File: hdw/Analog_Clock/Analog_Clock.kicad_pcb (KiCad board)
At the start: 2 copper layers, 427 parts, among them J1301 USB_B_Mini, J201 +12V IN, J2401 I2C, J2402 USB UART, J2403 DAC SPI, J801 PICKIT4, Q1601 BSS214NW, Q2401 BSS214NW, Q401 BSS214NW, Q402 ZXMS6004FFTA, Q601 FDC5612, Q801 BSS214NW, SW2201 Cap_Touch, SW2202 Cap_Touch, SW801 MRST, U1001 PIC32MZ0512EFE064T-I_PT, U1201 DS3231MZ, U1301 TLV6700, U1302 FT234XD, U1303 74LVC1G17, U1304 TXB0102DCU, U1305 TPD3S014DBVR, U1401 INA219BxDCN, U1402 MCP9804, U1501 DS1683, U1601 74LVC1G06, U1602 74LVC1G06, U1603 LP2985-3.3, U1604 74LVC1G06, U1605 74LVC1G07, U1606 74LVC1G06, U1701 74LVC1G06, U1702 74LVC1G06, U1703 74LVC1G06, U1704 74LVC1G06, U1801 74LVC1G07, U1802 LT1790-2.048, U1803 DAC8551, U1804 OPA2197xDGK, U1901 74LVC1G07, U1902 LT1790-2.048, U1903 DAC8551, U1904 OPA2197xDGK, U2001 74LVC1G07, U2002 LT1790-2.048, U2003 DAC8551, U2004 OPA2197xDGK, U201 TPS26600RHFT, U2101 LP5009, U2201 AT42QT1010-TSHR, U2202 AT42QT1010-TSHR, U2203 74LVC1G17, U2204 74LVC1G17, U2301 74LVC1G06, U2302 74LVC1G06, U2303 74LVC1G06, U2304 74LVC1G06, U2401 LTC6900, U2402 74LVC1G08, U2403 MCP9804, U301 INA219BxDCN, U302 MCP9804, U401 TPS62150, U501 INA219BxDCN, U502 MCP9804, U601 TLV6700, U602 LT3757, U701 INA219BxDCN, U702 MCP9804, X1101 ASE-8.000MHz, X1102 ECS-327KE

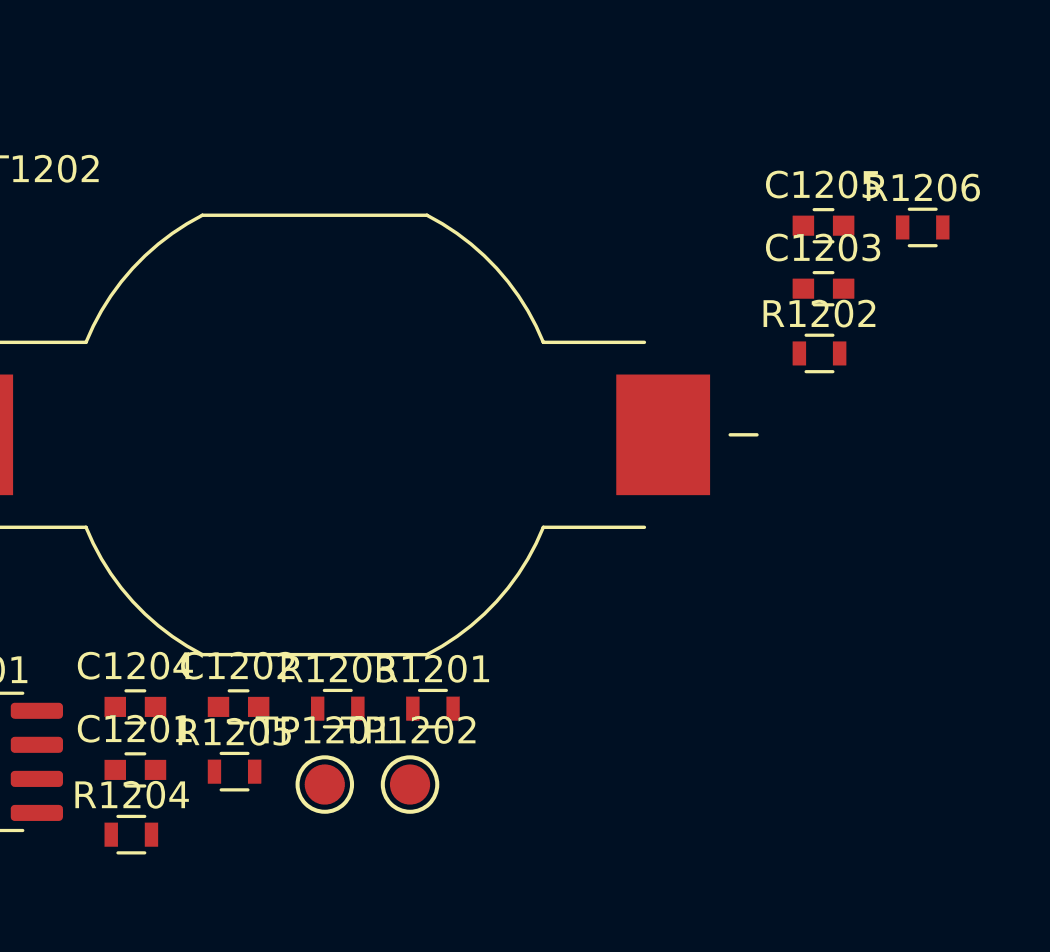
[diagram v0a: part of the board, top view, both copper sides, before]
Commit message: Changed VBAT ADC circuit
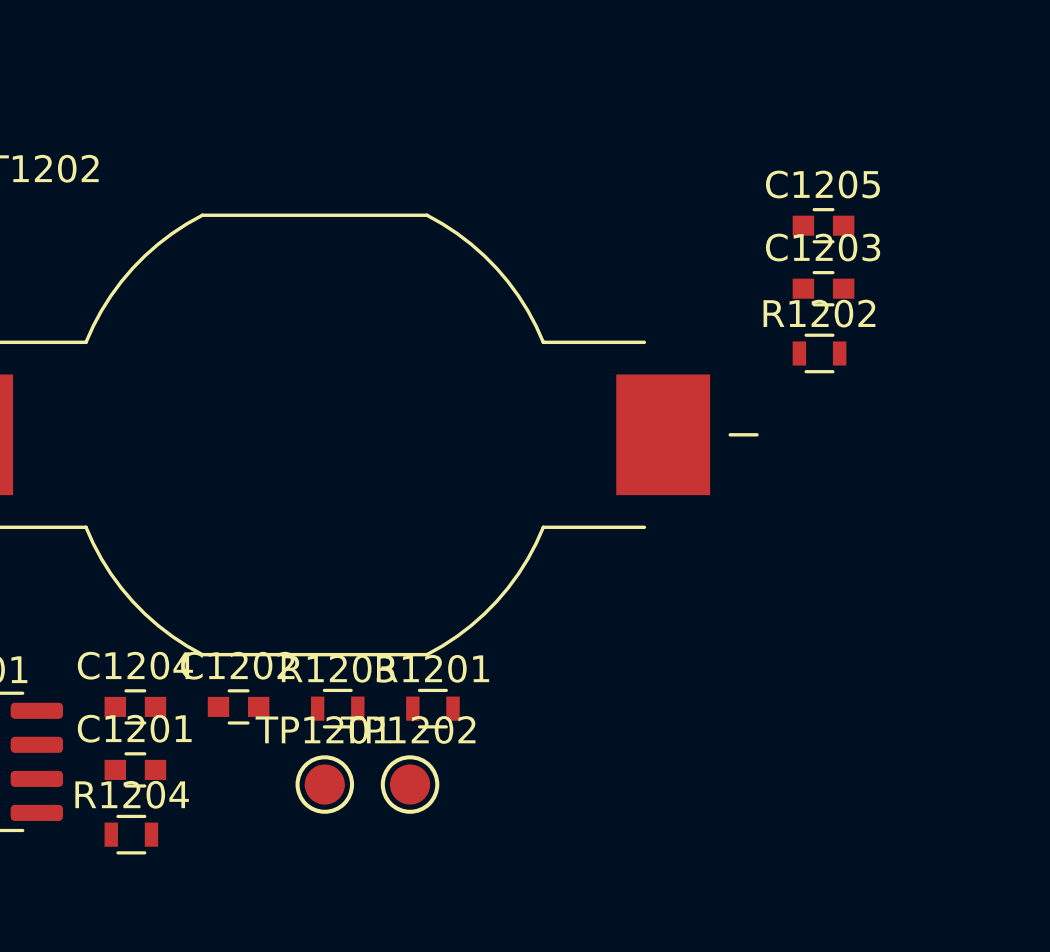
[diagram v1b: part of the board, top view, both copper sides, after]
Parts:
- removed R1205, R1206: 562k, Resistors_SMD:R_0603
- R1201: value 105k -> 1.07M
- R1202: value 22k -> 220k
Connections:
- R1201 pad 2: Net-(R1201-Pad2) -> VBAT_ADC
- R1202 pad 1: Net-(R1201-Pad2) -> VBAT_ADC

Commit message: started arranging parts on PCB
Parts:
- moved C903 335.0 mm to (72.4, 143.4), turned to 90 degrees
- moved C906 334.8 mm to (76.4, 143.4), turned to 90 degrees
- moved L901 332.6 mm to (80.9, 156.4), turned to 270 degrees
- moved C921 332.0 mm to (81.7, 151.7)
- moved L902 332.0 mm to (82.5, 156.4), turned to 270 degrees
- moved C904 331.6 mm to (75.1, 143.4), turned to 90 degrees
- moved C919 324.5 mm to (81.7, 153.0)
- moved C920 321.3 mm to (82.5, 136.1)
- moved C917 320.6 mm to (81.7, 154.4)
- moved C902 320.4 mm to (84.8, 154.4), turned to 180 degrees
- moved C907 320.3 mm to (84.8, 151.7), turned to 180 degrees
- moved C901 319.6 mm to (73.7, 143.4), turned to 90 degrees
- moved C916 317.6 mm to (82.5, 133.4)
- moved C909 316.5 mm to (85.5, 132.1), turned to 180 degrees
- moved C905 316.4 mm to (84.8, 153.0), turned to 180 degrees
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
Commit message: more PCB grouping
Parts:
- added MES1801: Voltmeter_DC, Custom Footprints Library:SO-45_Panel_Meter, F.Cu at (401.4, -55.2)
- added MES1901: Voltmeter_DC, Custom Footprints Library:SO-45_Panel_Meter, F.Cu at (401.4, 1.23)
- added MES2001: Voltmeter_DC, Custom Footprints Library:SO-45_Panel_Meter, F.Cu at (499.3, -55.2)
- added REF**: Symbol_Barrel_Polarity, Symbol:Symbol_Barrel_Polarity, F.Cu at (33.3, 126.8)
- added U1202: TLV6700, TO_SOT_Packages_SMD:SOT-23-6, F.Cu at (69.0, 89.9)
- C301, C302, C303, C501, C502, C503, C801, D201, D801, Q801, R1001, R1002, R1101, R1102, R1106, R1107, R801, R802, R803, R804, R805, U301, U302, U501, U502: moved to B.Cu
- moved C1203 553.2 mm to (31.6, 82.4), turned to 270 degrees
- moved TP1202 538.3 mm to (29.6, 79.6)
- moved R1204 525.8 mm to (31.6, 79.6), turned to 90 degrees
- moved C1205 522.6 mm to (63.4, 90.2), turned to 90 degrees
- moved C1202 521.1 mm to (40.8, 83.4), turned to 270 degrees
- moved R1202 520.5 mm to (64.8, 90.2), turned to 90 degrees
- moved C1201 515.7 mm to (42.2, 83.4), turned to 270 degrees
- moved U1201 515.5 mm to (36.2, 82.0)
- moved R1201 503.5 mm to (66.2, 90.2), turned to 270 degrees
- moved BT1202 501.5 mm to (63.0, 67.8)
- moved TP1201 501.5 mm to (63.4, 80.9)
- moved R1203 497.0 mm to (69.0, 87.3), turned to 180 degrees
- moved C1204 489.9 mm to (69.0, 92.5), turned to 180 degrees
- moved R201 446.2 mm to (40.6, 120.0)
- moved R203 443.1 mm to (41.1, 122.0), turned to 270 degrees
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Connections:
- D801 pad 1: Net-(D801-Pad1) -> +3V3
- D801 pad 3: +3V3 -> Net-(D801-Pad3)
- D801 pad 4: PIC32MZ_ICSPDAT -> Net-(D801-Pad4)
- D801 pad 6: Net-(D801-Pad6) -> PIC32MZ_ICSPDAT
- J801 pad 1: Net-(D801-Pad1) -> Net-(D801-Pad3)
- L801 pad 2: Net-(D801-Pad1) -> Net-(D801-Pad3)
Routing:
- net Net-(C201-Pad2): track 0.00 -> 1.41 mm
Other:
- board text added: "+"
- board text added: "+12V"
- board text added: "+12VIN"
- board text added: "+3.3V"
- board text added: "+VBAT"
- board text added: "-"
- board text added: "BCKP RTC REFCLK"
- board text added: "REFCLK1"
- board text added: "RTCCCLK"

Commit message: Arranged more components on PCB
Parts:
- removed R1101, R1204, R1316: 10k, Resistors_SMD:R_0603
- removed TP1101, TP1202: TP, Custom Footprints Library:Test_Point
- C1301, C1302, C1303, C1305, C1307, C1309, C1311, C2201, C2202, C2205, C2206, C2207, C2208, R1307, R1311, R1312, R1601, R1603, U1302, U1303, U1304: moved to B.Cu
- moved R1701 441.2 mm to (101.6, 60.4), turned to 270 degrees
- moved R1705 435.3 mm to (101.6, 71.8), turned to 90 degrees
- moved R1704 435.2 mm to (107.3, 64.6)
- moved C1701 434.9 mm to (104.0, 61.8), turned to 180 degrees
- moved R1706 434.7 mm to (101.6, 77.7), turned to 270 degrees
- moved R1707 433.7 mm to (107.3, 70.4)
- moved R1702 433.7 mm to (101.6, 66.0), turned to 270 degrees
- moved R2102 431.7 mm to (137.7, 71.1), turned to 90 degrees
- moved C1704 431.3 mm to (104.0, 79.0), turned to 180 degrees
- moved R1703 430.9 mm to (107.3, 58.9)
- moved C1702 430.5 mm to (104.0, 67.5), turned to 180 degrees
- moved R2301 429.5 mm to (102.0, 26.4), turned to 270 degrees
- moved C2101 429.5 mm to (136.2, 71.1), turned to 90 degrees
- moved R1708 429.1 mm to (107.3, 76.1)
- moved D1702 427.5 mm to (107.3, 66.1)
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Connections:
- BT1202 pad 1: (no net) -> VBAT
- BT1202 pad 2: (no net) -> GND
- R1306 pad 2: USB_UART_TX -> USB_UART_RX
- R1308 pad 2: USB_UART_RX -> USB_UART_TX
- R1314 pad 2: USB_UART_RX_BUF -> USB_UART_TX_BUF
- R1315 pad 2: USB_UART_TX_BUF -> USB_UART_RX_BUF
- U1001 pad 46: PIC32MZ_RTCC_CLK -> Net-(U1001-Pad46)
- U1201 pad 1: Backup_RTC_REFCLK -> Net-(U1201-Pad1)
- U1304 pad 1: USB_UART_TX_BUF -> USB_UART_RX_BUF
- U1304 pad 4: USB_UART_TX -> USB_UART_RX
- U1304 pad 5: USB_UART_RX -> USB_UART_TX
- U1304 pad 8: USB_UART_RX_BUF -> USB_UART_TX_BUF
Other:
- board text added: "+5V USB"
- board text added: "Function"
- board text added: "Power"
- board text added: "TX/RX"
- board text removed: "BCKP RTC REFCLK"
- board text removed: "RTCCCLK"

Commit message: More PCB arrangement
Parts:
- removed C1304, C1305, C1306, C1310, C1312, C1313, C1401, C1402, C1403: 0.1uF, Capacitors_SMD:C_0603
- removed C1308: 10uF, Capacitors_SMD:C_0603
- removed L1301: 600R 0.5A, Inductors_SMD:L_0603
- removed R1302: 487k, Resistors_SMD:R_0603
- removed R1303: 6.04k, Resistors_SMD:R_0603
- removed R1304: 40.2k, Resistors_SMD:R_0603
- removed R1305: 10k, Resistors_SMD:R_0603
- removed R1306, R1308: 100k, Resistors_SMD:R_0603
- removed R1307: 1k, Resistors_SMD:R_0603
- removed R1309, R1313: 10, Resistors_SMD:R_0603
- removed R1310: 0.02, Resistors_SMD:R_0612
- removed REF**: Symbol_Barrel_Polarity, Symbol:Symbol_Barrel_Polarity
- removed TP1301: TP, Custom Footprints Library:Test_Point
- removed U1303: 74LVC1G17, TO_SOT_Packages_SMD:SOT-353_SC-70-5
- removed U1304: TXB0102DCU, Package_SO:VSSOP-8_2.4x2.1mm_P0.5mm
- removed U1305: TPD3S014DBVR, TO_SOT_Packages_SMD:SOT-23-6
- removed U1401: INA219BxDCN, Package_TO_SOT_SMD:SOT-23-8
- removed U1402: MCP9804, Package_DFN_QFN:DFN-8-1EP_3x2mm_P0.5mm_EP1.3x1.5mm
- C1303: footprint Capacitors_SMD:C_0805 -> Capacitors_SMD:C_0603
- C1801, C1802, C1803, C1804, C1805, C1806, C1811, D1801, L1801, R1801, R1802, R1803, R1806, R1808, R1809, R1810, R1811, R1812, TP1801, TP1901, TP2001, U1801, U1802, U1803, U1804: moved to B.Cu
- R1314, R1315: value 100k -> 10k
- U1301: value TLV6700 -> TPD2EUSB30A; footprint Package_TO_SOT_SMD:SOT-23-6 -> Package_TO_SOT_SMD:Texas_DRT-3
- moved C2012 449.3 mm to (57.5, 186.2), turned to 180 degrees
- moved C1912 394.5 mm to (57.5, 187.6), turned to 180 degrees
- moved C1812 377.0 mm to (57.5, 189.0), turned to 180 degrees
- moved MES1801 250.2 mm to (376.0, 193.7)
- moved MES2001 250.0 mm to (476.0, 193.7)
- moved C2402 241.4 mm to (373.7, -47.9)
- moved D2401 241.4 mm to (360.2, -48.7)
- moved J2401 241.4 mm to (370.2, -60.1)
- moved R2402 241.4 mm to (381.0, -46.6)
- moved R2407 241.4 mm to (381.0, -49.0)
- moved BZ2401 241.4 mm to (362.6, -57.7)
- moved C2403 241.4 mm to (383.8, -56.6)
- moved J2402 241.4 mm to (374.9, -60.1)
- moved J2403 241.4 mm to (379.5, -60.1)
- moved R2401 241.4 mm to (378.8, -51.5)
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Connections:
- C1301 pad 1: +3.3V_USB -> +3V3
- C1302 pad 1: +5V_USB -> +3V3
- C1303 pad 1: +5V_USB -> +3V3
- C1307 pad 1: +3.3V_USB -> +3V3
- R1301 pad 1: +5V_USB -> +3V3
- R1314 pad 1: +3.3V_USB -> +3V3
- R1314 pad 2: USB_UART_TX_BUF -> USB_UART_RX
- R1315 pad 1: +3.3V_USB -> +3V3
- R1315 pad 2: USB_UART_RX_BUF -> USB_UART_TX
- U1301 pad 1: POS5_USB_PGOOD -> /USB UART Bridge/CONN_USB+
- U1301 pad 2: GND -> /USB UART Bridge/CONN_USB-
- U1301 pad 3: Net-(R1302-Pad2) -> GND
- U1302 pad 10: USB_UART_TX_BUF -> USB_UART_TX
- U1302 pad 3: +3.3V_USB -> +3V3
- U1302 pad 4: +5V_USB -> +3V3
- U1302 pad 7: USB_UART_RX_BUF -> USB_UART_RX
- U1302 pad 9: +3.3V_USB -> +3V3

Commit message: Major USB restructuring
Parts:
- added C1304: 0.1uF, Capacitors_SMD:C_0603, B.Cu at (43.0, 29.9)
- added C1306: 0.1uF, Capacitors_SMD:C_0603, F.Cu at (48.6, 20.7)
- added C1310: 0.1uF, Capacitors_SMD:C_0603, F.Cu at (50.2, 23.0)
- added C1312: 0.1uF, Capacitors_SMD:C_0603, F.Cu at (50.2, 27.9)
- added C1401: 0.1uF, Capacitors_SMD:C_0603, B.Cu at (47.9, 29.4)
- added C1402: 0.1uF, Capacitors_SMD:C_0603, B.Cu at (51.2, 32.1)
- added C1403: 0.1uF, Capacitors_SMD:C_0603, F.Cu at (54.7, 32.2)
- added L1301: 600R 0.5A, Inductors_SMD:L_0603, F.Cu at (39.7, 23.0)
- added R1302: 487k, Resistors_SMD:R_0603, F.Cu at (46.2, 32.0)
- added R1303: 6.04k, Resistors_SMD:R_0603, F.Cu at (45.7, 29.9)
- added R1304: 40.2k, Resistors_SMD:R_0603, F.Cu at (46.2, 27.8)
- added R1305: 10k, Resistors_SMD:R_0603, F.Cu at (43.0, 27.1)
- added R1306: 100k, Resistors_SMD:R_0603, F.Cu at (51.5, 24.9)
- added R1308: 100k, Resistors_SMD:R_0603, F.Cu at (51.5, 26.4)
- added R1309: 10, Resistors_SMD:R_0603, F.Cu at (46.9, 24.7)
- added R1310: 0.02, Resistors_SMD:R_0612, F.Cu at (46.3, 21.3)
- added R1313: 10, Resistors_SMD:R_0603, F.Cu at (45.5, 24.7)
- added TP1301: TP, Custom Footprints Library:Test_Point, F.Cu at (51.0, 20.7)
- added U1304: TXB0102DCU, Package_SO:VSSOP-8_2.4x2.1mm_P0.5mm, B.Cu at (50.2, 25.7)
- added U1305: TPD3S014DBVR, TO_SOT_Packages_SMD:SOT-23-6, F.Cu at (42.7, 21.2)
- added U1401: INA219BxDCN, Package_TO_SOT_SMD:SOT-23-8, B.Cu at (48.5, 32.1)
- added U1402: MCP9804, Package_DFN_QFN:DFN-8-1EP_3x2mm_P0.5mm_EP1.3x1.5mm, F.Cu at (55.4, 30.1)
- C1602, C1603, C1605, C1606, C1607, C1701, C1702, C1703, C1704, C2301, C2302, C2303, C2304, D2401, Q2401, R1701, R1702, R1705, R1706, R2301, R2302, R2305, R2306, R2402, R2405, R2407: moved to B.Cu
- R1314, R1315: value 10k -> 100k
- U1301: value TPD2EUSB30A -> TLV6700; footprint Package_TO_SOT_SMD:Texas_DRT-3 -> Package_TO_SOT_SMD:SOT-23-6
- moved C1801 247.1 mm to (125.6, 164.9)
- moved C1802 247.1 mm to (144.4, 163.3)
- moved C1803 247.1 mm to (125.6, 170.1)
- moved C1804 247.1 mm to (130.9, 175.1)
- moved C1805 247.1 mm to (125.6, 171.7)
- moved C1806 247.1 mm to (130.9, 173.5)
- moved C1808 247.1 mm to (133.3, 166.8)
- moved C1809 247.1 mm to (133.3, 165.4)
- moved C1810 247.1 mm to (133.3, 164.1)
- moved C1901 247.1 mm to (175.6, 164.9)
- moved C1902 247.1 mm to (194.4, 163.3)
- moved C1903 247.1 mm to (175.6, 170.1)
- moved C1904 247.1 mm to (180.9, 175.1)
- moved C1905 247.1 mm to (175.6, 171.7)
- moved C1906 247.1 mm to (180.9, 173.5)
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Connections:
- C1301 pad 1: +3V3 -> +3.3V_USB
- C1302 pad 1: +3V3 -> +5V_USB
- C1303 pad 1: +3V3 -> +5V_USB
- C1307 pad 1: +3V3 -> +3.3V_USB
- R1301 pad 1: +3V3 -> +5V_USB
- R1314 pad 1: +3V3 -> +3.3V_USB
- R1314 pad 2: USB_UART_RX -> USB_UART_RX_BUF
- R1315 pad 1: +3V3 -> +3.3V_USB
- R1315 pad 2: USB_UART_TX -> USB_UART_TX_BUF
- U1301 pad 1: /USB UART Bridge/CONN_USB+ -> POS5_USB_PGOOD
- U1301 pad 2: /USB UART Bridge/CONN_USB- -> GND
- U1301 pad 3: GND -> Net-(R1302-Pad2)
- U1302 pad 10: USB_UART_TX -> USB_UART_TX_BUF
- U1302 pad 3: +3V3 -> +3.3V_USB
- U1302 pad 4: +3V3 -> +5V_USB
- U1302 pad 7: USB_UART_RX -> USB_UART_RX_BUF
- U1302 pad 9: +3V3 -> +3.3V_USB
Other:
- board text added: "+20V"
- board text added: "+5V_USB"
- board text added: "Alarm Arm"
- board text added: "CPU Trap"
- board text added: "DAC SPI"
- board text added: "DAC0 VREF"
- board text added: "DAC1 VREF"
- board text added: "DAC2 VREF"
- board text added: "Date"
- board text added: "Error"
- board text added: "GND"
- board text added: "Heart Beat"
- board text added: "I2C"
- board text added: "MOSI"
- board text added: "PGOOD:"
- board text added: "RX"
- board text added: "Reset"
- board text added: "SCL"
- board text added: "SCLK"
- board text added: "SDA"
- board text added: "TX"
- board text added: "Time"
- board text added: "USB UART"
- board text added: "VBAT"
- board text added: "Weekday"
- board text removed: "+5V USB"

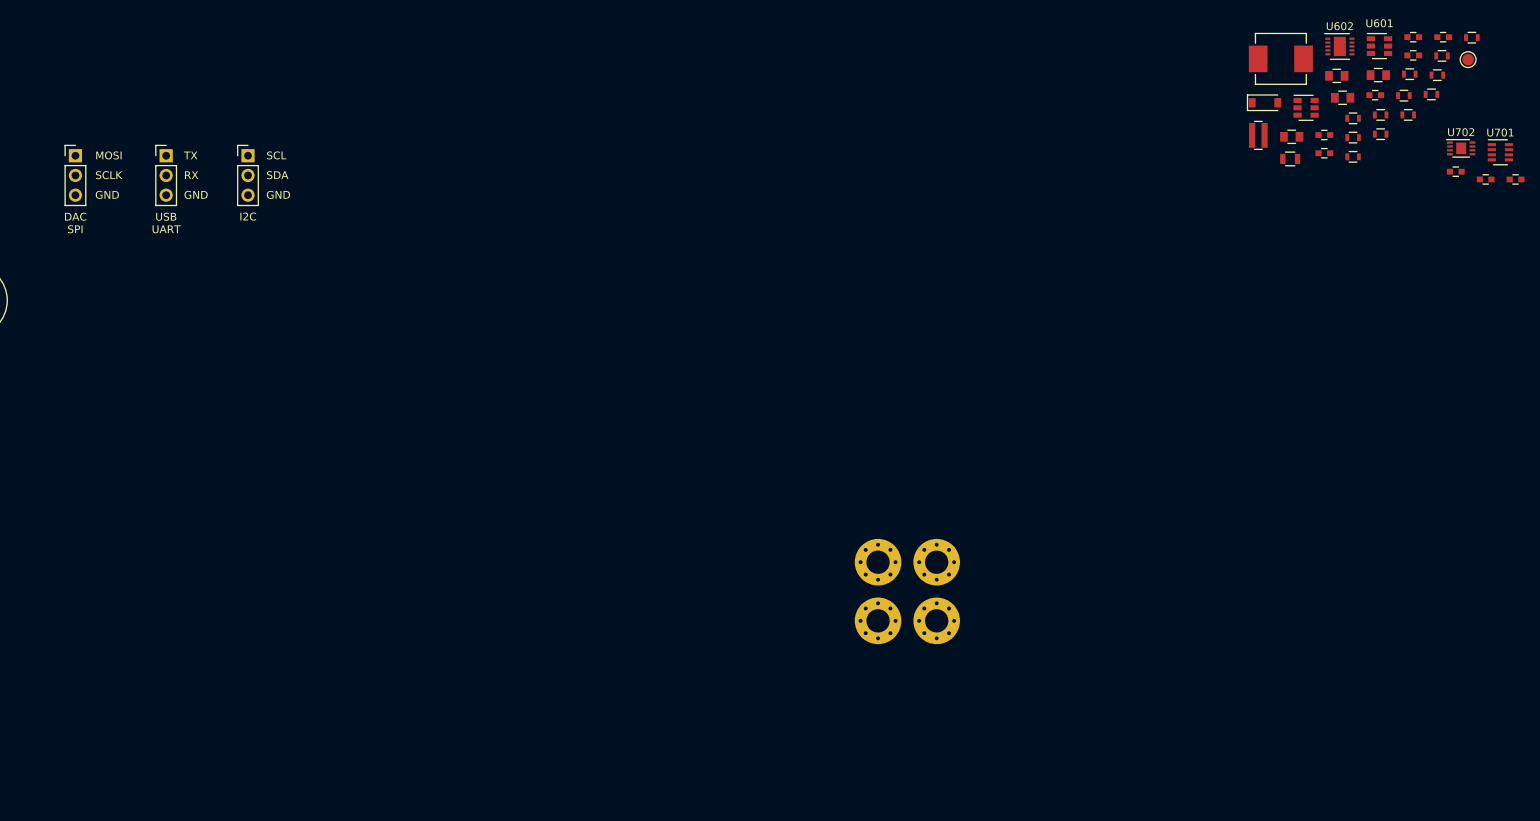
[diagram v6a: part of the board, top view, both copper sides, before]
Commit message: Finished arranging parts, few netlist changes
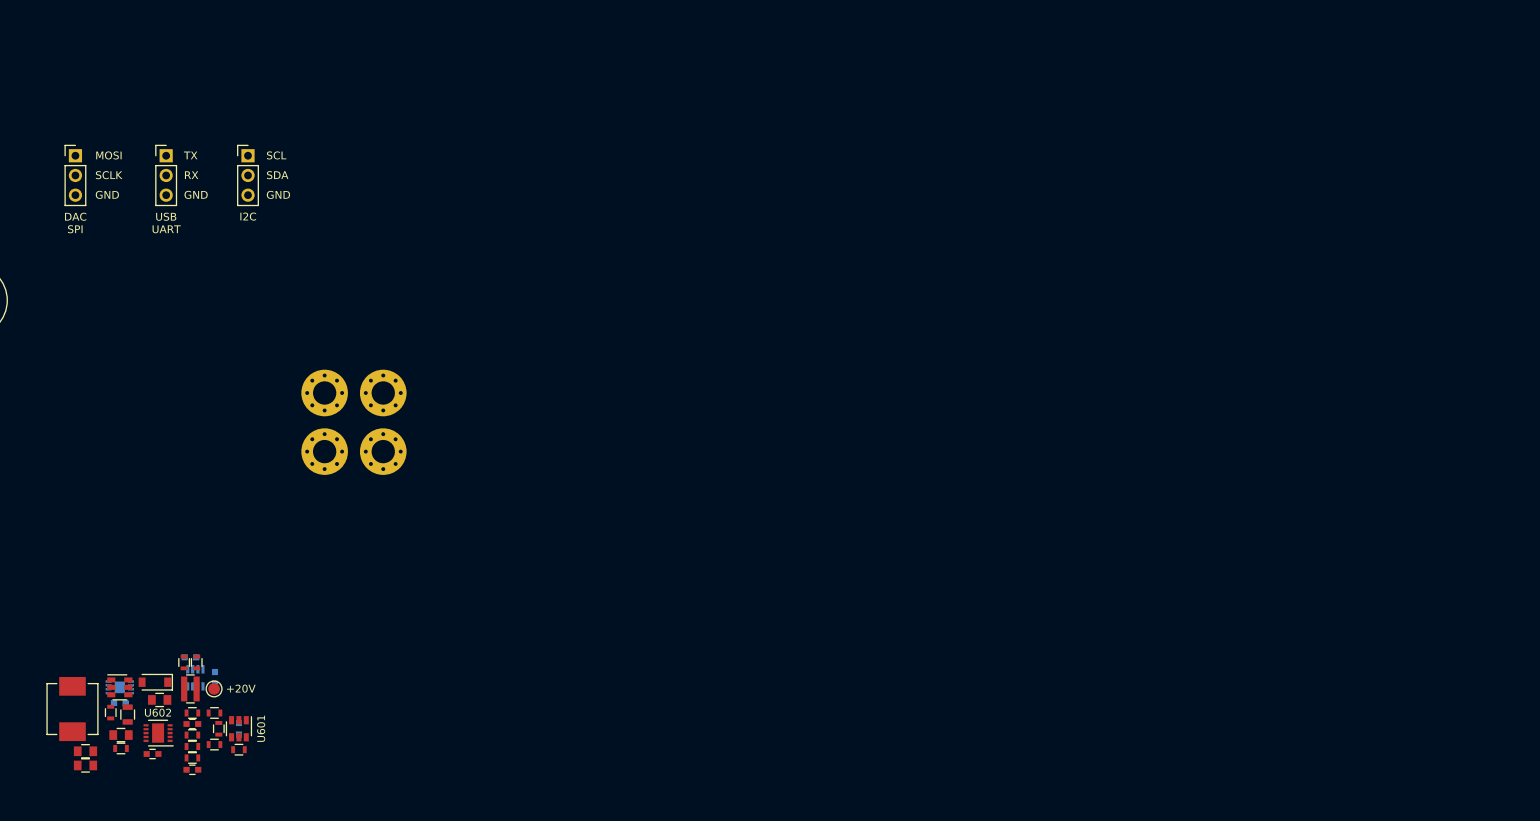
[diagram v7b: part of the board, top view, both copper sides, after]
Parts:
- removed C608: 10nF, Capacitors_SMD:C_0603
- removed C609: 1nF, Capacitors_SMD:C_0603
- C606, C701, C702, C703, U701, U702: moved to B.Cu
- R610, R612: value 100 -> 10
- moved C602 188.8 mm to (200.8, 102.7)
- moved R605 187.3 mm to (205.4, 100.5), turned to 180 degrees
- moved U702 186.2 mm to (205.2, 92.7)
- moved C703 185.2 mm to (205.2, 94.7), turned to 180 degrees
- moved R607 183.4 mm to (220.6, 100.7), turned to 180 degrees
- moved C601 182.5 mm to (200.8, 100.9)
- moved C701 181.4 mm to (214.3, 88.8)
- moved U701 181.2 mm to (215.0, 91.4), turned to 270 degrees
- moved TP601 180.7 mm to (217.4, 92.9)
- moved R613 179.7 mm to (214.6, 98.8), turned to 180 degrees
- moved R601 179.3 mm to (217.4, 96.0)
- moved C604 178.9 mm to (209.4, 101.2)
- moved R610 178.2 mm to (213.5, 89.5), turned to 90 degrees
- moved L601 176.7 mm to (199.1, 95.5), turned to 90 degrees
- moved R614 176.5 mm to (214.6, 100.3)
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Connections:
- R610 pad 1: POS20_SNS+ -> Net-(C610-Pad1)
- R610 pad 2: Net-(C610-Pad1) -> POS20_SNS+
- R612 pad 1: POS20_SNS- -> +20V
- R612 pad 2: +20V -> POS20_SNS-
